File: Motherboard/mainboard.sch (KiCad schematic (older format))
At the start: 50 parts, among them IC1 BMX160, J1 Conn_01x01, J2 10118194-0001LF, J28 Conn_01x01, J29 Conn_01x01, J3 Micro_SD_Card, J30 Conn_01x01, J4 xf2m-2415-1a, J5 XF2M-1015-1A, J6 U.FL-R-SMT-1, J7 U.FL-R-SMT-1, J8 Conn_01x01, SW1 KMR231NG LFS, U1 RFM95W-915S2, U2 ATSAMD51G_TQFN48, U3 DRV8848, U4 TPS82740BSIPR, U5 DRV8848, U6 MAX708RESA-T, U8 RFM95W-915S2

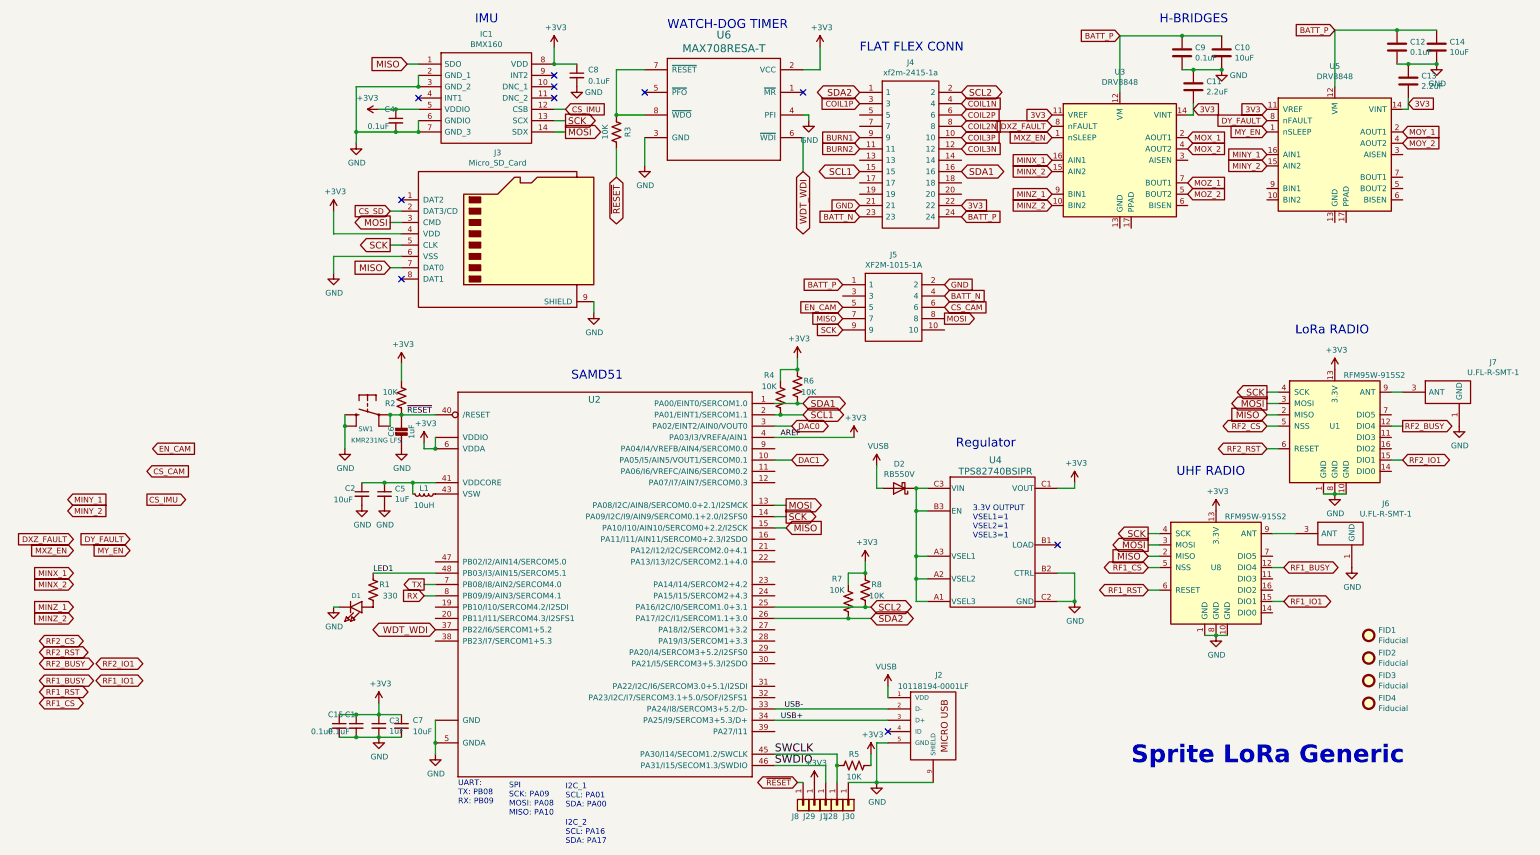
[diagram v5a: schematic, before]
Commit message: ~75% routed
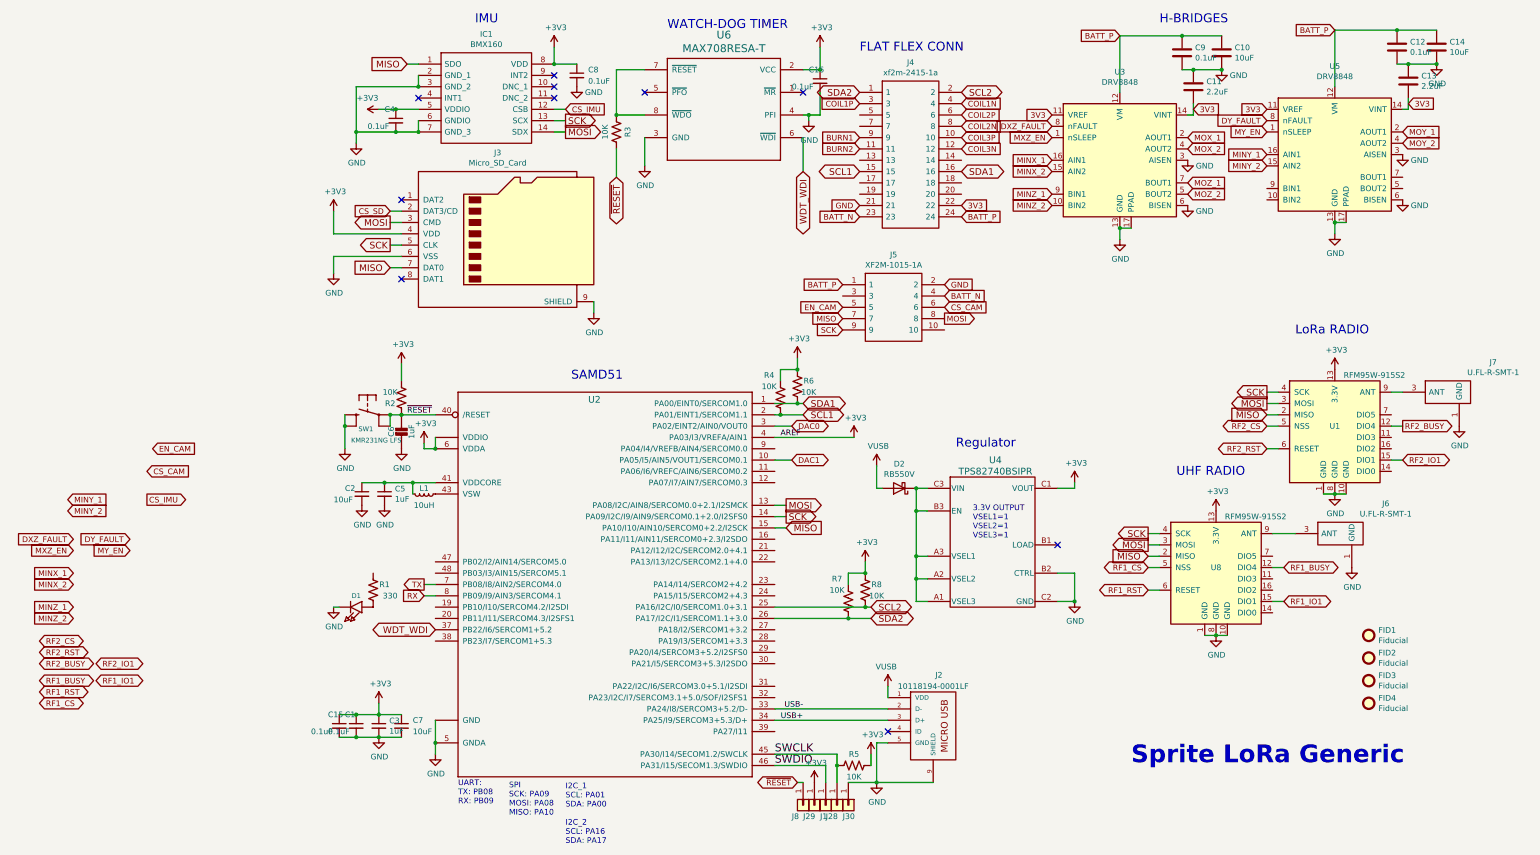
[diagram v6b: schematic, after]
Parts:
- added C16: 0.1uF, Capacitor_SMD:C_0402_1005Metric, symbol mainboard-rescue:C_Small-Device
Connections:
- net +3V3: now also C16.1
- net GND: now also U3.13 (GND), U3.17 (PPAD), U3.3 (AISEN), U3.6 (BISEN), U5.13 (GND), U5.17 (PPAD), U5.3 (AISEN), U5.6 (BISEN), C16.2
- net LED1: no longer names the net of R1.2
- net LED1: no longer U2.48 (PB03/I3/AIN15/SERCOM5.1)
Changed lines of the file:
@@
 Text Label 4700 6700 2    50   ~ 0
 USB-
-Text Label 900  5500 0    50   ~ 0
-LED1
 NoConn ~ 5450 6900
 $Comp
@@
 	-1   0    0    -1
 $EndComp
-Wire Wire Line
-	900  5500 1450 5500
 $Comp
 L mainboard-rescue:R_US-Device R1
@@
 Text GLabel -1100 4850 2    50   Output ~ 0
 CS_IMU
+$Comp
+L power:GND #PWR0129
+U 1 1 5DCE9737
+P 8100 2250
+F 0 "#PWR0129" H 8100 2000 50  0001 C CNN
+F 1 "GND" H 8250 2200 50  0000 C CNN
+F 2 "" H 8100 2250 50  0001 C CNN
+F 3 "" H 8100 2250 50  0001 C CNN
+	1    8100 2250
+	1    0    0    -1
+$EndComp
+$Comp
+L power:GND #PWR0128
+U 1 1 5DCE2BBF
+P 8100 1850
+F 0 "#PWR0128" H 8100 1600 50  0001 C CNN
+F 1 "GND" H 8250 1800 50  0000 C CNN
+F 2 "" H 8100 1850 50  0001 C CNN
+F 3 "" H 8100 1850 50  0001 C CNN
+	1    8100 1850
+	1    0    0    -1
+$EndComp
+$Comp
+L power:GND #PWR0132
+U 1 1 5DD0AEF2
+P 10000 1800
+F 0 "#PWR0132" H 10000 1550 50  0001 C CNN
+F 1 "GND" H 10150 1750 50  0000 C CNN
+F 2 "" H 10000 1800 50  0001 C CNN
+F 3 "" H 10000 1800 50  0001 C CNN
+	1    10000 1800
+	1    0    0    -1
+$EndComp
+$Comp
+L power:GND #PWR0133
+U 1 1 5DD0AEF9
+P 10000 2200
+F 0 "#PWR0133" H 10000 1950 50  0001 C CNN
+F 1 "GND" H 10150 2150 50  0000 C CNN
+F 2 "" H 10000 2200 50  0001 C CNN
+F 3 "" H 10000 2200 50  0001 C CNN
+	1    10000 2200
+	1    0    0    -1
+$EndComp
+Wire Wire Line
+	7600 2450 7500 2450
+Wire Wire Line
+	9500 2400 9400 2400
+Connection ~ 9400 2400
+Wire Wire Line
+	9400 2500 9400 2400
+$Comp
+L power:GND #PWR0131
+U 1 1 5DD0AED6
+P 9400 2500
+F 0 "#PWR0131" H 9400 2250 50  0001 C CNN
+F 1 "GND" H 9405 2327 50  0000 C CNN
+F 2 "" H 9400 2500 50  0001 C CNN
+F 3 "" H 9400 2500 50  0001 C CNN
+	1    9400 2500
+	1    0    0    -1
+$EndComp
+Connection ~ 7500 2450
+Wire Wire Line
+	7500 2550 7500 2450
+$Comp
+L power:GND #PWR0125
+U 1 1 5DC582A1
+P 7500 2550
+F 0 "#PWR0125" H 7500 2300 50  0001 C CNN
+F 1 "GND" H 7505 2377 50  0000 C CNN
+F 2 "" H 7500 2550 50  0001 C CNN
+F 3 "" H 7500 2550 50  0001 C CNN
+	1    7500 2550
+	1    0    0    -1
+$EndComp
+$Comp
+L mainboard-rescue:C_Small-Device C16
+U 1 1 5DBB39D1
+P 4850 1150
+F 0 "C16" H 4750 1250 50  0000 L CNN
+F 1 "0.1uF" H 4600 1100 50  0000 L CNN
+F 2 "Capacitor_SMD:C_0402_1005Metric" H 4850 1150 50  0001 C CNN
+F 3 "~" H 4850 1150 50  0001 C CNN
+	1    4850 1150
+	1    0    0    -1
+$EndComp
+Connection ~ 4850 1050
+Wire Wire Line
+	4850 1250 4850 1450
+Wire Wire Line
+	4850 1450 4750 1450
+Connection ~ 4750 1450
 $EndSCHEMATC

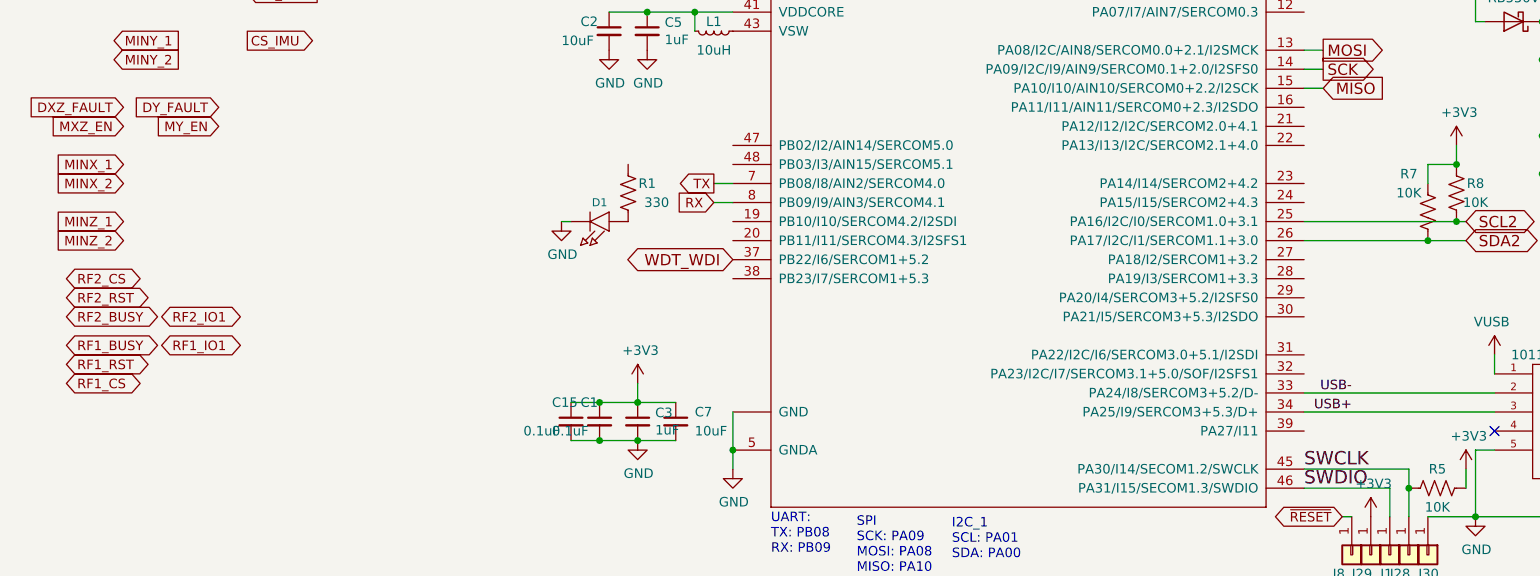
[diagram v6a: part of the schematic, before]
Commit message: routing ~80%
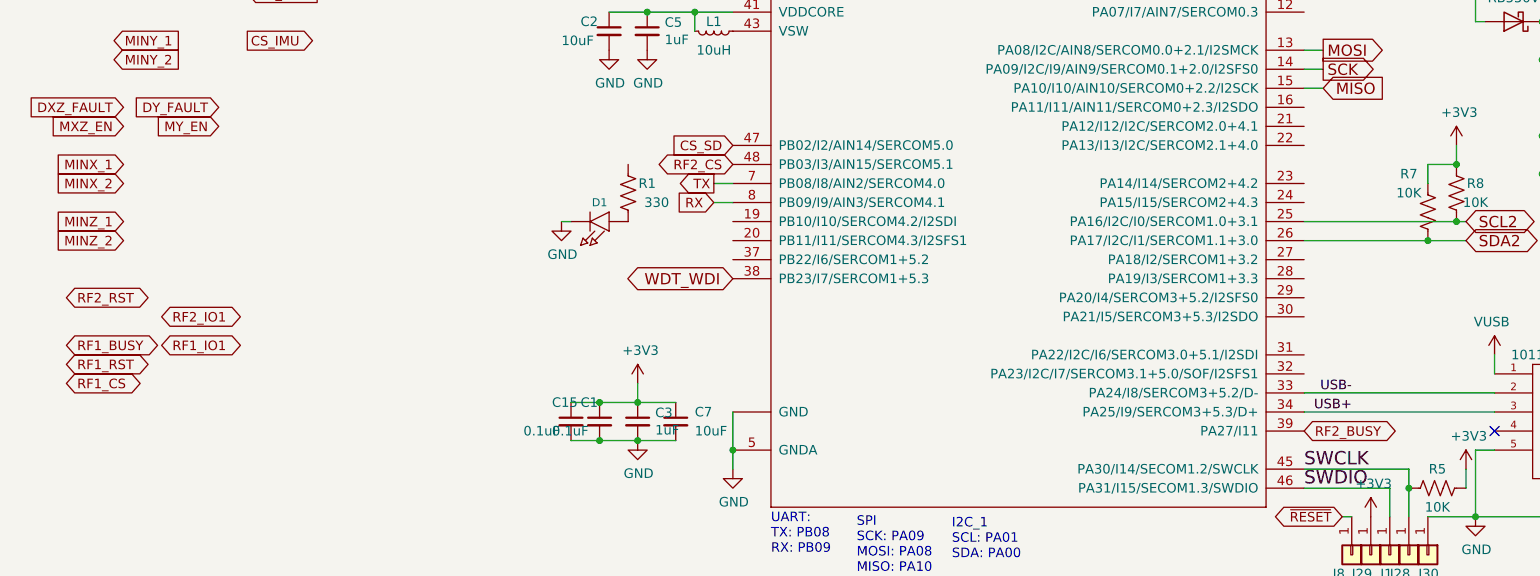
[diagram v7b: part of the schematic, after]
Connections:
- net CS_SD: now also U2.47 (PB02/I2/AIN14/SERCOM5.0)
- net RF2_BUSY: now also U2.39 (PA27/I11)
- net RF2_CS: now also U2.48 (PB03/I3/AIN15/SERCOM5.1)
- net WDT_WDI: now also U2.38 (PB23/I7/SERCOM1+5.3); no longer U2.37 (PB22/I6/SERCOM1+5.2)
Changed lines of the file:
@@
 Text GLabel 5050 2950 0    50   Input ~ 0
 BATT_P
-Text GLabel 1450 6000 0    59   BiDi ~ 0
+Text GLabel 1450 6100 0    59   BiDi ~ 0
 WDT_WDI
 Text GLabel 7500 750  0    50   Input ~ 0
@@
 Wire Wire Line
 	8800 4200 8900 4200
-Text GLabel -2050 6100 2    50   BiDi ~ 0
+Text GLabel 1450 5500 0    50   BiDi ~ 0
 RF2_CS
 Text GLabel -1550 6300 2    50   BiDi ~ 0
@@
 Text GLabel -2050 6200 2    50   BiDi ~ 0
 RF2_RST
-Text GLabel -2050 6300 2    50   BiDi ~ 0
+Text GLabel 4450 6900 2    50   BiDi ~ 0
 RF2_BUSY
 Text GLabel 10000 4500 2    50   BiDi ~ 0
@@
 	4850 1450 4750 1450
 Connection ~ 4750 1450
+Text GLabel 1450 5400 0    50   Input ~ 0
+CS_SD
 $EndSCHEMATC
